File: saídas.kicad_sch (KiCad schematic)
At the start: 36 parts, among them J10 CARGA_12V, J12 Habilita buzzer, J13 Habilita rele, J6 MOTOR, J7 PWM_SERVO, J8 PWM_SERVO, J9 Screw_Terminal_01x03, K1 Relay_SPDT_Latching_1coil, Q1 2N7002, Q2 SI4483ADY-T1-GE3, Q3 2N7002, Q4 2N7002, U6 AS4950

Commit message: organização e legendas do esquemático
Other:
- moved on the sheet: BZ1, C10, C11, D10, D4, D5, D6, D7, D8, D9, J10, J12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

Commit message: style: ajustes no layout
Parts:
- added D12: LED, LED_THT:LED_D5.0mm, symbol Device:LED
- added R36: 0603WAF1201T5E, jlclib:R0603, symbol a_jlclib:0603WAF1201T5E
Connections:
- net GND: now also R36.1
- net IN5_PWM: now also D12.2 (A)
- new net: D12.1 (K), R36.2

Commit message: ajustes no layout e serigrafia
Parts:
- removed D12: LED, LED_THT:LED_D5.0mm, symbol Device:LED
- removed D7: SS12 Schottky, Diode_SMD:D_SMA_Handsoldering, symbol Device:D_Schottky
- removed J10: CARGA_12V, Connector_PinSocket_2.54mm:PinSocket_1x02_P2.54mm_Vertical, symbol Connector:Conn_01x02_Pin
- removed J6: MOTOR, Connector_PinSocket_2.54mm:PinSocket_1x02_P2.54mm_Vertical, symbol Connector:Conn_01x02_Pin
- removed R36: 0603WAF1201T5E, jlclib:R0603, symbol a_jlclib:0603WAF1201T5E
- added J6: MOTOR, TerminalBlock:TerminalBlock_MaiXu_MX126-5.0-02P_1x02_P5.00mm, symbol Connector:Screw_Terminal_01x02
- added R37: 15R10W, Resistor_THT:R_Axial_Power_L38.0mm_W9.0mm_P40.64mm, symbol Device:R
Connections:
- net 5V_IN: no longer C10.1, C11.1, J7.2 (Pin_2), J8.2 (Pin_2)
- net GND: now also R37.2
- net at U6.6 (OUT1): now also J6.2 (Pin_2)
- net at U6.8 (OUT2): now also J6.1 (Pin_1)
- net at D8.2 (A), Q2.5 (D), Q2.6 (D)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: now also R37.1
- new net 5V_IN_SERVO: C10.1, C11.1, J7.2 (Pin_2), J8.2 (Pin_2)

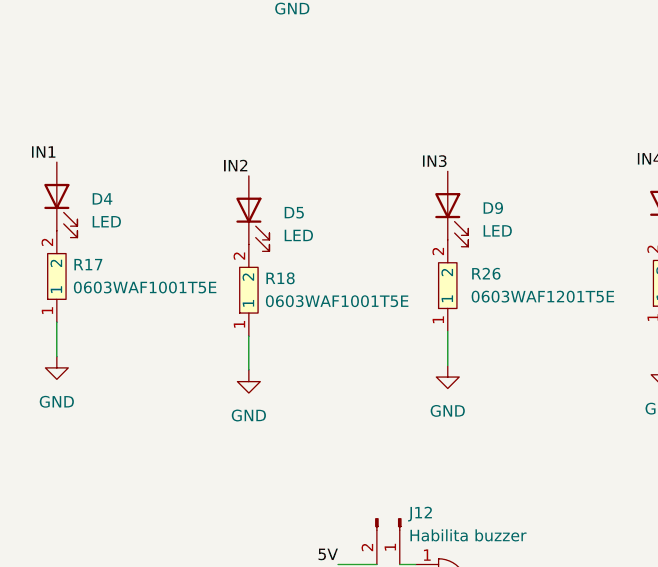
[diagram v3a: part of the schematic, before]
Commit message: ajusta circuitos de entrada, alimentação e saída e adiciona visualizações da PCB
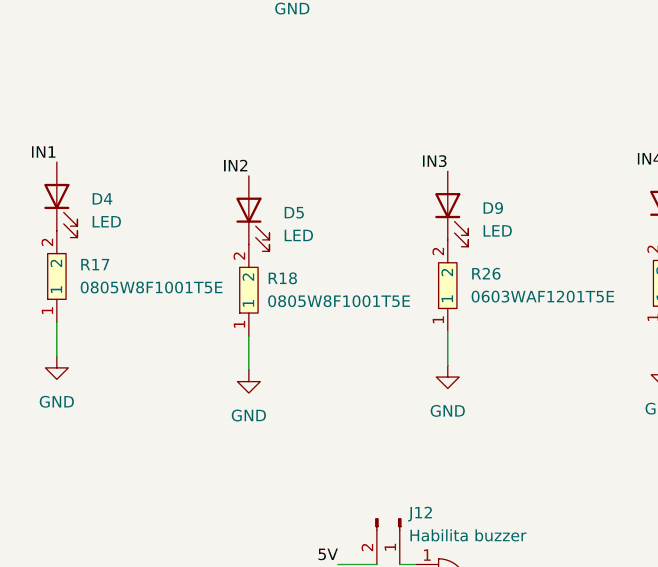
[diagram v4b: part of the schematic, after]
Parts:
- removed R17, R18: 0603WAF1001T5E, jlclib:R0603, symbol a_jlclib:0603WAF1001T5E
- added R17, R18: 0805W8F1001T5E, jlclib:R0805, symbol a_jlclib:0805W8F1001T5E
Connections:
- net GND: now also R17.1, R18.1
- net at D4.1 (K): now also R17.2
- net at D5.1 (K): now also R18.2
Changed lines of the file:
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@@
 	)
 	(symbol
+		(lib_id "a_jlclib:0805W8F1001T5E")
+		(at 24.892 101.346 90)
+		(unit 1)
+		(exclude_from_sim no)
+		(in_bom yes)
+		(on_board yes)
+		(dnp no)
+		(fields_autoplaced yes)
+		(property "Reference" "R17"
+			(at 27.432 100.0759 90)
+			(effects
+				(font
+					(size 1.27 1.27)
+				)
+				(justify right)
+			)
+		)
+		(property "Value" "0805W8F1001T5E"
+			(at 27.432 102.6159 90)
+			(effects
+				(font
+					(size 1.27 1.27)
+				)
+				(justify right)
+			)
+		)
+		(property "Footprint" "jlclib:R0805"
+			(at 32.512 101.346 0)
+			(effects
+				(font
+					(size 1.27 1.27)
+				)
+				(hide yes)
+			)
+		)
+		(property "Datasheet" "https://lcsc.com/product-detail/Chip-Resistor-Surface-Mount-UniOhm_1KR-1001-1_C17513.html"
+			(at 35.052 101.346 0)
+			(effects
+				(font
+					(size 1.27 1.27)
+				)
+				(hide yes)
+			)
+		)
+		(property "Description" "1KΩ (1001) ±1%"
+			(at 24.892 101.346 0)
+			(effects
+				(font
+					(size 1.27 1.27)
+				)
+				(hide yes)
+			)
+		)
+		(property "Manufacturer" "UNI-ROYAL(厚声)"
+			(at 37.592 101.346 0)
+			(effects
+				(font
+					(size 1.27 1.27)
+				)
+				(hide yes)
+			)
+		)
+		(property "MPN" "0805W8F1001T5E"
+			(at 40.132 101.346 0)
+			(effects
+				(font
+					(size 1.27 1.27)
+				)
+				(hide yes)
+			)
+		)
+		(property "LCSC Part" "C17513"
+			(at 42.672 101.346 0)
+			(effects
+				(font
+					(size 1.27 1.27)
+				)
+				(hide yes)
+			)
+		)
+		(pin "2"
+		)
+		(pin "1"
+		)
+		(instances
+			(project "pcb-moduloDidaticoSCADA"
+				(path "/d871af36-cd7a-4e62-8016-cc5e63560ec7/4eb53ab9-9d45-4380-91d5-f64cda0bd8d0"
+					(reference "R17")
+					(unit 1)
+				)
+			)
+		)
+	)
+	(symbol
 		(lib_id "Device:LED")
 		(at 24.892 92.456 90)
@@
 	)
 	(symbol
-		(lib_id "a_jlclib:0603WAF1001T5E")
-		(at 24.892 101.346 90)
-		(unit 1)
-		(exclude_from_sim no)
-		(in_bom yes)
-		(on_board yes)
-		(dnp no)
-		(fields_autoplaced yes)
-		(property "Reference" "R17"
-			(at 26.67 100.0759 90)
-			(effects
-				(font
-					(size 1.27 1.27)
-				)
-				(justify right)
-			)
-		)
-		(property "Value" "0603WAF1001T5E"
-			(at 26.67 102.6159 90)
-			(effects
-				(font
-					(size 1.27 1.27)
-				)
-				(justify right)
-			)
-		)
-		(property "Footprint" "jlclib:R0603"
-			(at 32.512 101.346 0)
-			(effects
-				(font
-					(size 1.27 1.27)
-				)
-				(hide yes)
-			)
-		)
-		(property "Datasheet" "https://lcsc.com/product-detail/Chip-Resistor-Surface-Mount-UniOhm_1KR-1001-1_C21190.html"
-			(at 35.052 101.346 0)
-			(effects
-				(font
-					(size 1.27 1.27)
-				)
-				(hide yes)
-			)
-		)
-		(property "Description" "1KΩ (1001) ±1%"
-			(at 24.892 101.346 0)
-			(effects
-				(font
-					(size 1.27 1.27)
-				)
-				(hide yes)
-			)
-		)
-		(property "Manufacturer" "UNI-ROYAL(厚声)"
-			(at 37.592 101.346 0)
-			(effects
-				(font
-					(size 1.27 1.27)
-				)
-				(hide yes)
-			)
-		)
-		(property "MPN" "0603WAF1001T5E"
-			(at 40.132 101.346 0)
-			(effects
-				(font
-					(size 1.27 1.27)
-				)
-				(hide yes)
-			)
-		)
-		(property "LCSC Part" "C21190"
-			(at 42.672 101.346 0)
-			(effects
-				(font
-					(size 1.27 1.27)
-				)
-				(hide yes)
-			)
-		)
-		(pin "1"
-		)
-		(pin "2"
-		)
-		(instances
-			(project ""
-				(path "/d871af36-cd7a-4e62-8016-cc5e63560ec7/4eb53ab9-9d45-4380-91d5-f64cda0bd8d0"
-					(reference "R17")
-					(unit 1)
-				)
-			)
-		)
-	)
-	(symbol
 		(lib_id "a_jlclib:0603WAF1201T5E")
 		(at 153.924 48.514 90)
@@
 	)
 	(symbol
-		(lib_id "a_jlclib:0603WAF1001T5E")
-		(at 46.228 102.87 90)
-		(unit 1)
-		(exclude_from_sim no)
-		(in_bom yes)
-		(on_board yes)
-		(dnp no)
-		(fields_autoplaced yes)
-		(property "Reference" "R18"
-			(at 48.006 101.5999 90)
-			(effects
-				(font
-					(size 1.27 1.27)
-				)
-				(justify right)
-			)
-		)
-		(property "Value" "0603WAF1001T5E"
-			(at 48.006 104.1399 90)
-			(effects
-				(font
-					(size 1.27 1.27)
-				)
-				(justify right)
-			)
-		)
-		(property "Footprint" "jlclib:R0603"
-			(at 53.848 102.87 0)
-			(effects
-				(font
-					(size 1.27 1.27)
-				)
-				(hide yes)
-			)
-		)
-		(property "Datasheet" "https://lcsc.com/product-detail/Chip-Resistor-Surface-Mount-UniOhm_1KR-1001-1_C21190.html"
-			(at 56.388 102.87 0)
-			(effects
-				(font
-					(size 1.27 1.27)
-				)
-				(hide yes)
-			)
-		)
-		(property "Description" "1KΩ (1001) ±1%"
-			(at 46.228 102.87 0)
-			(effects
-				(font
-					(size 1.27 1.27)
-				)
-				(hide yes)
-			)
-		)
-		(property "Manufacturer" "UNI-ROYAL(厚声)"
-			(at 58.928 102.87 0)
-			(effects
-				(font
-					(size 1.27 1.27)
-				)
-				(hide yes)
-			)
-		)
-		(property "MPN" "0603WAF1001T5E"
-			(at 61.468 102.87 0)
-			(effects
-				(font
-					(size 1.27 1.27)
-				)
-				(hide yes)
-			)
-		)
-		(property "LCSC Part" "C21190"
-			(at 64.008 102.87 0)
-			(effects
-				(font
-					(size 1.27 1.27)
-				)
-				(hide yes)
-			)
-		)
-		(pin "1"
-		)
-		(pin "2"
-		)
-		(instances
-			(project "pcb-moduloDidaticoSCADA"
-				(path "/d871af36-cd7a-4e62-8016-cc5e63560ec7/4eb53ab9-9d45-4380-91d5-f64cda0bd8d0"
-					(reference "R18")
-					(unit 1)
-				)
-			)
-		)
-	)
-	(symbol
 		(lib_id "power:+5VA")
 		(at 125.73 148.59 270)
@@
 					(unit 1)
 				)
+			)
+		)
+	)
+	(symbol
+		(lib_id "a_jlclib:0805W8F1001T5E")
+		(at 46.228 102.87 90)
+		(unit 1)
+		(exclude_from_sim no)
+		(in_bom yes)
+		(on_board yes)
+		(dnp no)
+		(fields_autoplaced yes)
+		(property "Reference" "R18"
+			(at 48.26 101.5999 90)
+			(effects
+				(font
+					(size 1.27 1.27)
+				)
+				(justify right)
+			)
+		)
+		(property "Value" "0805W8F1001T5E"
+			(at 48.26 104.1399 90)
+			(effects
+				(font
+					(size 1.27 1.27)
+				)
+				(justify right)
+			)
+		)
+		(property "Footprint" "jlclib:R0805"
+			(at 53.848 102.87 0)
+			(effects
+				(font
+					(size 1.27 1.27)
+				)
+				(hide yes)
+			)
+		)
+		(property "Datasheet" "https://lcsc.com/product-detail/Chip-Resistor-Surface-Mount-UniOhm_1KR-1001-1_C17513.html"
+			(at 56.388 102.87 0)
+			(effects
+				(font
+					(size 1.27 1.27)
+				)
+				(hide yes)
+			)
+		)
+		(property "Description" "1KΩ (1001) ±1%"
+			(at 46.228 102.87 0)
+			(effects
+				(font
+					(size 1.27 1.27)
+				)
+				(hide yes)
+			)
+		)
+		(property "Manufacturer" "UNI-ROYAL(厚声)"
+			(at 58.928 102.87 0)
+			(effects
+				(font
+					(size 1.27 1.27)
+				)
+				(hide yes)
+			)
+		)
+		(property "MPN" "0805W8F1001T5E"
+			(at 61.468 102.87 0)
+			(effects
+				(font
+					(size 1.27 1.27)
+				)
+				(hide yes)
+			)
+		)
+		(property "LCSC Part" "C17513"
+			(at 64.008 102.87 0)
+			(effects
+				(font
+					(size 1.27 1.27)
+				)
+				(hide yes)
+			)
+		)
+		(pin "2"
+		)
+		(pin "1"
+		)
+		(instances
+			(project "pcb-moduloDidaticoSCADA"
+				(path "/d871af36-cd7a-4e62-8016-cc5e63560ec7/4eb53ab9-9d45-4380-91d5-f64cda0bd8d0"
+					(reference "R18")
+					(unit 1)
+				)
